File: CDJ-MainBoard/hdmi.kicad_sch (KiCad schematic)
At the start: 6 parts, among them J12 HR911130A, J13 PI HDMI_0 (HDMI_D_1.4 micro), J14 PI HDMI_0 (HDMI_D_1.4 micro), U1 Compute_Module_5_Functional

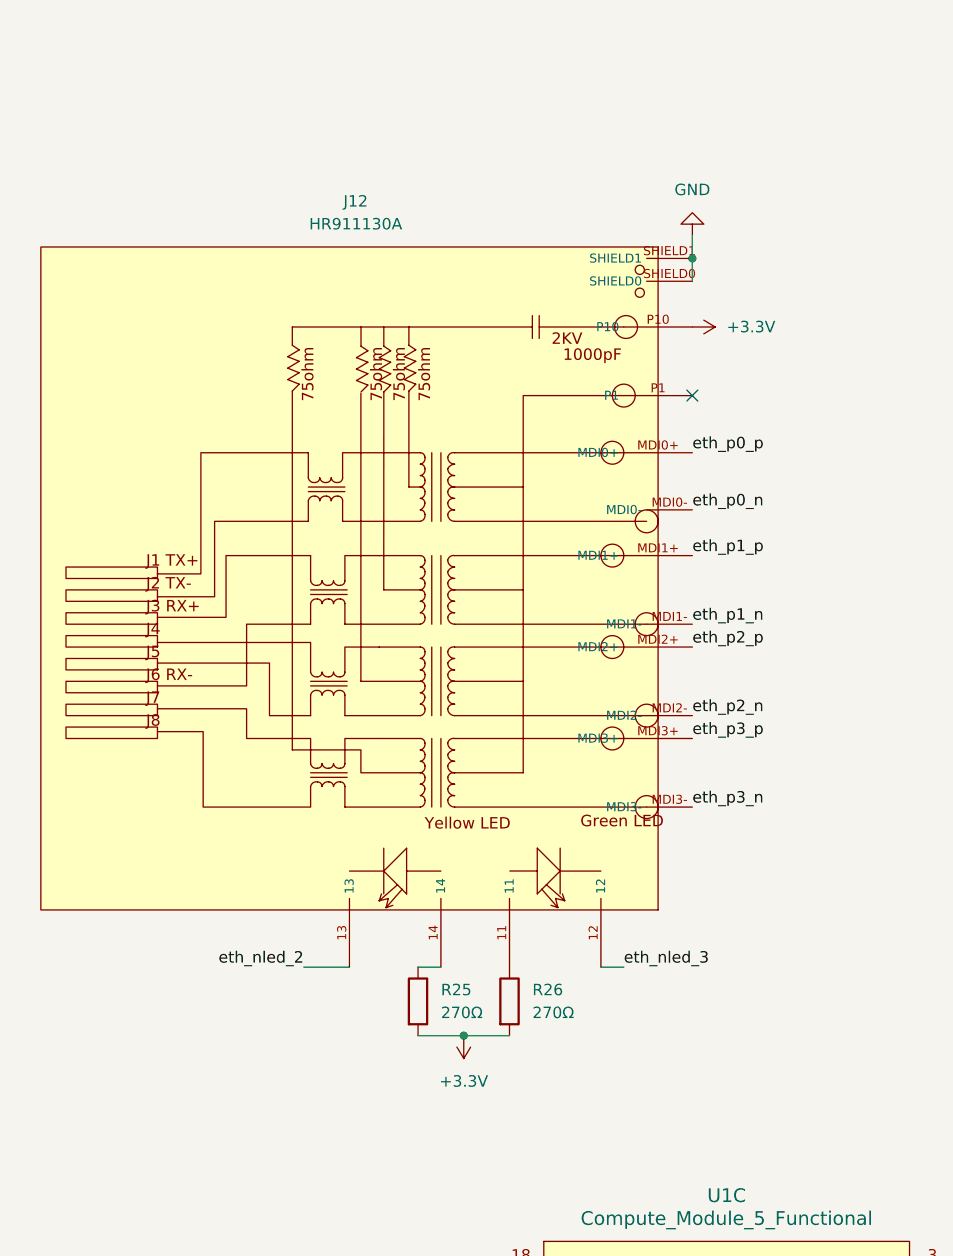
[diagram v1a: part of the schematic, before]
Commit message: Route the buck and fixed pinout on ethernet and 3D model offsets
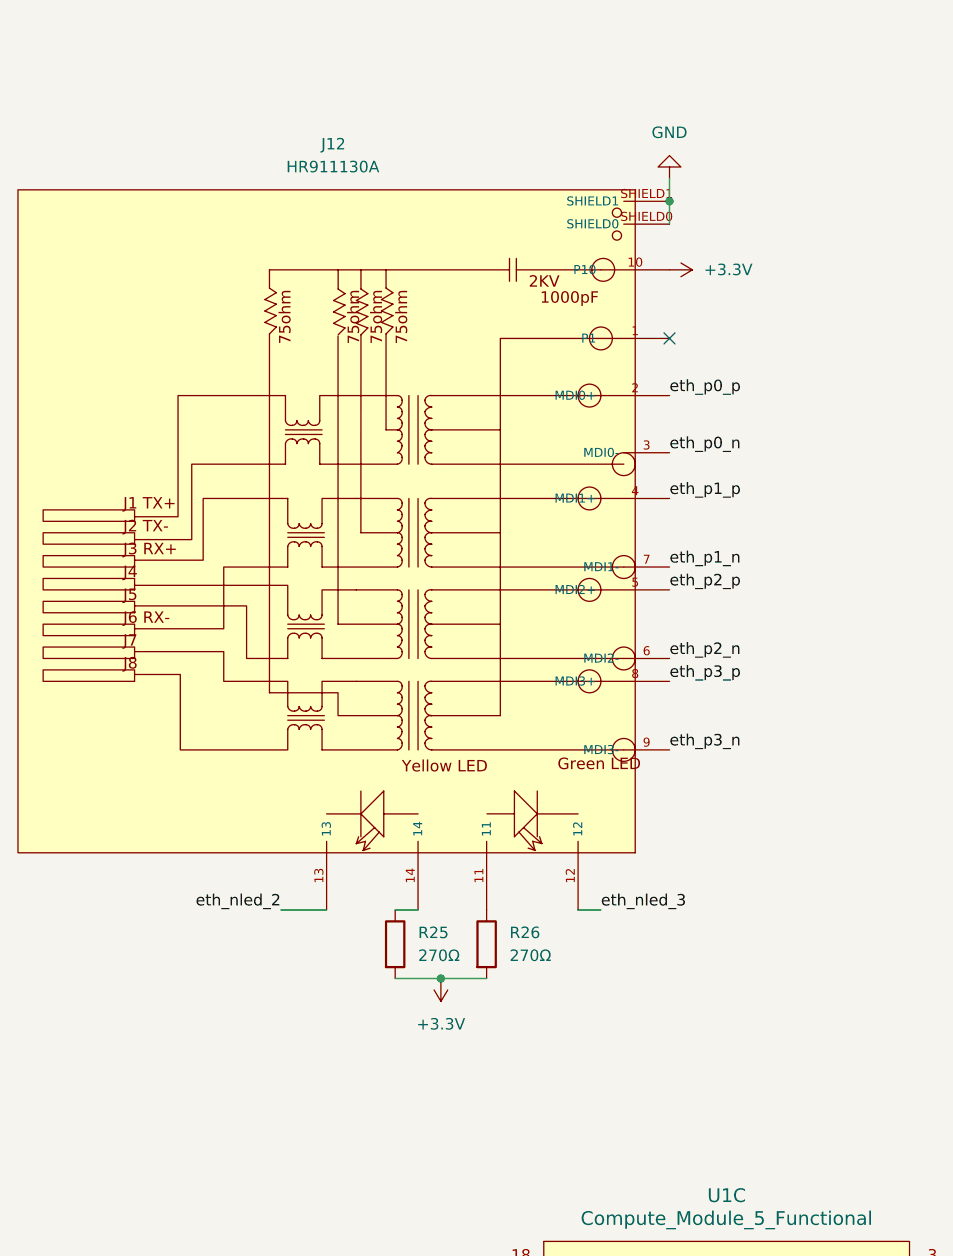
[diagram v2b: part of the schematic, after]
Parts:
- J12: footprint JLC2KiCad_lib-footprints:RJ45-TH_HR911130A -> JLC2KiCad_lib-footprints:RJ45-TH_HR911105A
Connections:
- net +3.3V: now also J12.10 (P10); no longer J12.P10
- net eth_p0_n: now also J12.3 (MDI0-); no longer J12.MDI0-
- net eth_p0_p: now also J12.2 (MDI0+); no longer J12.MDI0+
- net eth_p1_n: now also J12.7 (MDI1-); no longer J12.MDI1-
- net eth_p1_p: now also J12.4 (MDI1+); no longer J12.MDI1+
- net eth_p2_n: now also J12.6 (MDI2-); no longer J12.MDI2-
- net eth_p2_p: now also J12.5 (MDI2+); no longer J12.MDI2+
- net eth_p3_n: now also J12.9 (MDI3-); no longer J12.MDI3-
- net eth_p3_p: now also J12.8 (MDI3+); no longer J12.MDI3+
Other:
- moved on the sheet: R25, R26

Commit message: Route the ethernet port
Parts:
- J12: footprint JLC2KiCad_lib-footprints:RJ45-TH_HR911105A -> JLC2KiCad_lib-footprints:RJ45-TH_HR911130A
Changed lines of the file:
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@@
 			)
 		)
-		(property "Footprint" "JLC2KiCad_lib-footprints:RJ45-TH_HR911105A"
+		(property "Footprint" "JLC2KiCad_lib-footprints:RJ45-TH_HR911130A"
 			(at 67.31 59.69 0)
 			(effects
